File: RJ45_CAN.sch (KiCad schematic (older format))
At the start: 1 part, among them J1 RJ45

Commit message: Route, associate and generate bom and drawings.
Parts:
- J1: Farnell (none) -> 2135979
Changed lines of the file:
@@
 $Descr A4 11693 8268
 encoding utf-8
-Sheet 7 11
+Sheet 11 11
 Title ""
 Date "2021-02-26"
@@
 AR Path="/603AFD7E/603AEB0B" Ref="J9"  Part="1"
 AR Path="/603AFD80/603AEB0B" Ref="J10"  Part="1"
-F 0 "J6" H 5407 4367 50  0000 C CNN
+F 0 "J10" H 5407 4367 50  0000 C CNN
 F 1 "RJ45" H 5407 4276 50  0000 C CNN
 F 2 "Connector_RJ:RJ45_Amphenol_54602-x08_Horizontal" V 5350 3725 50  0001 C CNN
-F 3 "~" V 5350 3725 50  0001 C CNN
+F 3 "https://www.farnell.com/cad/1749592.pdf" V 5350 3725 50  0001 C CNN
+F 4 "2135979" H 5350 3700 50  0001 C CNN "Farnell"
 	1    5350 3700
 	1    0    0    -1

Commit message: Design v2 circuit and make footprints.
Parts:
- removed J1: RJ45, Connector_RJ:RJ45_Amphenol_54602-x08_Horizontal, symbol Connector:RJ45
- added J?: RJ45_Shielded, CAN-Distributor:RJHSE5480, symbol Connector:RJ45_Shielded
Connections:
- net labels added: CAN_SHLD
- net labels removed: CAN_V+, Reserved1, Reserved2, SHIELD
- wire segments 8 -> 7
- no-connect marks 0 -> 3
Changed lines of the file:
@@
 $Descr A4 11693 8268
 encoding utf-8
-Sheet 11 11
-Title ""
-Date "2021-02-26"
-Rev "1.0"
+Sheet 2 12
+Title "CAN Distributor"
+Date "2021-04-03"
+Rev "2.0"
 Comp ""
-Comment1 ""
+Comment1 "Designed by: Erik Almbratt"
 Comment2 ""
 Comment3 ""
 Comment4 ""
 $EndDescr
-$Comp
-L Connector:RJ45 J?
-U 1 1 603AEB0B
-P 5350 3700
-AR Path="/603AEB0B" Ref="J?"  Part="1"
-AR Path="/603ADFE4/603AEB0B" Ref="J1"  Part="1"
-AR Path="/603AF7AF/603AEB0B" Ref="J?"  Part="1"
-AR Path="/603AF7FC/603AEB0B" Ref="J2"  Part="1"
-AR Path="/603AF88D/603AEB0B" Ref="J3"  Part="1"
-AR Path="/603AF8B1/603AEB0B" Ref="J4"  Part="1"
-AR Path="/603AF8D1/603AEB0B" Ref="J5"  Part="1"
-AR Path="/603AF8E5/603AEB0B" Ref="J?"  Part="1"
-AR Path="/603AF91C/603AEB0B" Ref="J?"  Part="1"
-AR Path="/603AFD78/603AEB0B" Ref="J6"  Part="1"
-AR Path="/603AFD7A/603AEB0B" Ref="J7"  Part="1"
-AR Path="/603AFD7C/603AEB0B" Ref="J8"  Part="1"
-AR Path="/603AFD7E/603AEB0B" Ref="J9"  Part="1"
-AR Path="/603AFD80/603AEB0B" Ref="J10"  Part="1"
-F 0 "J10" H 5407 4367 50  0000 C CNN
-F 1 "RJ45" H 5407 4276 50  0000 C CNN
-F 2 "Connector_RJ:RJ45_Amphenol_54602-x08_Horizontal" V 5350 3725 50  0001 C CNN
-F 3 "https://www.farnell.com/cad/1749592.pdf" V 5350 3725 50  0001 C CNN
-F 4 "2135979" H 5350 3700 50  0001 C CNN "Farnell"
-	1    5350 3700
-	1    0    0    -1
-$EndComp
 Text GLabel 6100 4000 2    50   Input ~ 0
 CAN_H
@@
 CAN_GND
 Text GLabel 6100 3500 2    50   Input ~ 0
-SHIELD
-Text GLabel 6100 3700 2    50   Input ~ 0
-Reserved1
-Text GLabel 6100 3600 2    50   Input ~ 0
-Reserved2
-Text GLabel 6100 3300 2    50   Input ~ 0
-CAN_V+
-Wire Wire Line
-	6100 3300 5750 3300
+CAN_SHLD
 Wire Wire Line
 	5750 3400 6100 3400
 Wire Wire Line
 	6100 3500 5750 3500
-Wire Wire Line
-	5750 3600 6100 3600
-Wire Wire Line
-	6100 3700 5750 3700
 Wire Wire Line
 	5750 3800 6100 3800
@@
 Wire Wire Line
 	5750 4000 6100 4000
+NoConn ~ 5750 3300
+NoConn ~ 5750 3600
+NoConn ~ 5750 3700
+$Comp
+L Connector:RJ45_Shielded J?
+U 1 1 6068581B
+P 5350 3700
+AR Path="/603ADFE4/6068581B" Ref="J?"  Part="1"
+AR Path="/603AF7FC/6068581B" Ref="J?"  Part="1"
+AR Path="/603AF88D/6068581B" Ref="J?"  Part="1"
+AR Path="/603AF8B1/6068581B" Ref="J?"  Part="1"
+AR Path="/603AF8D1/6068581B" Ref="J?"  Part="1"
+AR Path="/603AFD78/6068581B" Ref="J?"  Part="1"
+AR Path="/603AFD7A/6068581B" Ref="J?"  Part="1"
+AR Path="/603AFD7C/6068581B" Ref="J?"  Part="1"
+AR Path="/603AFD7E/6068581B" Ref="J?"  Part="1"
+AR Path="/603AFD80/6068581B" Ref="J?"  Part="1"
+F 0 "J?" H 5350 4400 50  0000 C CNN
+F 1 "RJ45_Shielded" H 5350 4300 50  0000 C CNN
+F 2 "CAN-Distributor:RJHSE5480" V 5350 3725 50  0001 C CNN
+F 3 "https://www.farnell.com/cad/2360424.pdf" V 5350 3725 50  0001 C CNN
+F 4 "RJHSE5480" H 5350 3700 50  0001 C CNN "MPN"
+F 5 "3367703" H 5350 3700 50  0001 C CNN "Farnell"
+F 6 "AMPHENOL ICC" H 5350 3700 50  0001 C CNN "Manufacturer"
+	1    5350 3700
+	1    0    0    -1
+$EndComp
+Text GLabel 5500 4350 2    50   Input ~ 0
+CAN_SHLD
+Wire Wire Line
+	5350 4200 5350 4350
+Wire Wire Line
+	5350 4350 5500 4350
 $EndSCHEMATC

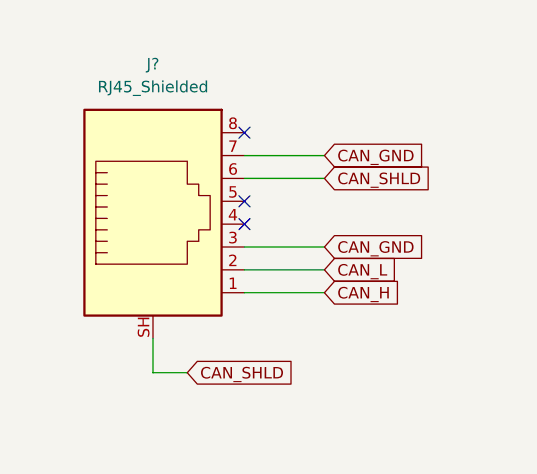
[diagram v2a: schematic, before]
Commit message: Perform layout. Add CAN testpoints.
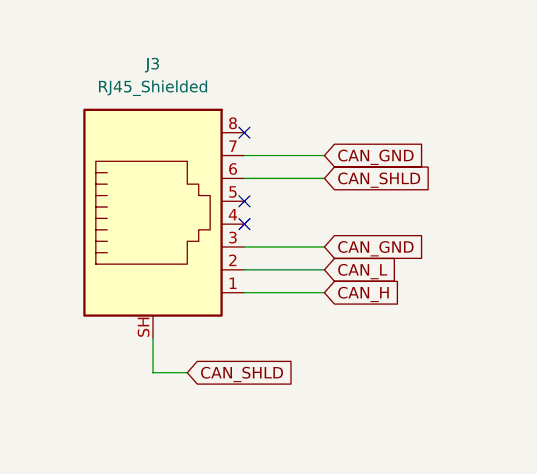
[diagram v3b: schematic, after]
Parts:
- gave numbers to parts that had none: 1
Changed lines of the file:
@@
 $Descr A4 11693 8268
 encoding utf-8
-Sheet 2 12
+Sheet 3 16
 Title "CAN Distributor"
 Date "2021-04-03"
@@
 NoConn ~ 5750 3700
 $Comp
-L Connector:RJ45_Shielded J?
+L Connector:RJ45_Shielded J2
 U 1 1 6068581B
 P 5350 3700
-AR Path="/603ADFE4/6068581B" Ref="J?"  Part="1"
-AR Path="/603AF7FC/6068581B" Ref="J?"  Part="1"
+AR Path="/603ADFE4/6068581B" Ref="J2"  Part="1"
+AR Path="/603AF7FC/6068581B" Ref="J3"  Part="1"
 AR Path="/603AF88D/6068581B" Ref="J?"  Part="1"
 AR Path="/603AF8B1/6068581B" Ref="J?"  Part="1"
@@
 AR Path="/603AFD7E/6068581B" Ref="J?"  Part="1"
 AR Path="/603AFD80/6068581B" Ref="J?"  Part="1"
-F 0 "J?" H 5350 4400 50  0000 C CNN
+F 0 "J3" H 5350 4400 50  0000 C CNN
 F 1 "RJ45_Shielded" H 5350 4300 50  0000 C CNN
 F 2 "CAN-Distributor:RJHSE5480" V 5350 3725 50  0001 C CNN

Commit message: Add protection TVS and GDT. Rename TP file.
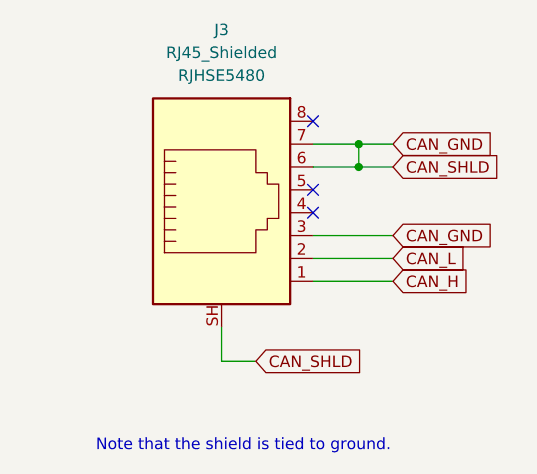
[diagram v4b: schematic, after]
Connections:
- net CAN_SHLD is gone; now on net CAN_GND: J2.6, J2.SH
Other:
- note added: "Note that the shield is tied to ground."
- moved on the sheet: J3
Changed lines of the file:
@@
 Sheet 3 16
 Title "CAN Distributor"
-Date "2021-04-03"
-Rev "2.0"
+Date "2021-04-04"
+Rev "2.1"
 Comp ""
 Comment1 "Designed by: Erik Almbratt"
@@
 Comment4 ""
 $EndDescr
-Text GLabel 6100 4000 2    50   Input ~ 0
-CAN_H
-Text GLabel 6100 3900 2    50   Input ~ 0
-CAN_L
-Text GLabel 6100 3800 2    50   Input ~ 0
+Text GLabel 6400 3750 2    50   Input ~ 0
 CAN_GND
-Text GLabel 6100 3400 2    50   Input ~ 0
+Text GLabel 6400 3350 2    50   Input ~ 0
 CAN_GND
-Text GLabel 6100 3500 2    50   Input ~ 0
-CAN_SHLD
 Wire Wire Line
-	5750 3400 6100 3400
-Wire Wire Line
-	6100 3500 5750 3500
-Wire Wire Line
-	5750 3800 6100 3800
-Wire Wire Line
-	6100 3900 5750 3900
-Wire Wire Line
-	5750 4000 6100 4000
-NoConn ~ 5750 3300
-NoConn ~ 5750 3600
-NoConn ~ 5750 3700
+	6050 3750 6400 3750
+NoConn ~ 6050 3250
+NoConn ~ 6050 3550
+NoConn ~ 6050 3650
 $Comp
 L Connector:RJ45_Shielded J2
 U 1 1 6068581B
-P 5350 3700
+P 5650 3650
 AR Path="/603ADFE4/6068581B" Ref="J2"  Part="1"
 AR Path="/603AF7FC/6068581B" Ref="J3"  Part="1"
@@
 AR Path="/603AFD7E/6068581B" Ref="J?"  Part="1"
 AR Path="/603AFD80/6068581B" Ref="J?"  Part="1"
-F 0 "J3" H 5350 4400 50  0000 C CNN
-F 1 "RJ45_Shielded" H 5350 4300 50  0000 C CNN
-F 2 "CAN-Distributor:RJHSE5480" V 5350 3725 50  0001 C CNN
-F 3 "https://www.farnell.com/cad/2360424.pdf" V 5350 3725 50  0001 C CNN
-F 4 "RJHSE5480" H 5350 3700 50  0001 C CNN "MPN"
-F 5 "3367703" H 5350 3700 50  0001 C CNN "Farnell"
-F 6 "AMPHENOL ICC" H 5350 3700 50  0001 C CNN "Manufacturer"
-	1    5350 3700
+F 0 "J3" H 5650 4450 50  0000 C CNN
+F 1 "RJ45_Shielded" H 5650 4350 50  0000 C CNN
+F 2 "CAN-Distributor:RJHSE5480" V 5650 3675 50  0001 C CNN
+F 3 "https://www.farnell.com/cad/2360424.pdf" V 5650 3675 50  0001 C CNN
+F 4 "RJHSE5480" H 5650 4250 50  0000 C CNN "MPN"
+F 5 "3367703" H 5650 3650 50  0001 C CNN "Farnell"
+F 6 "AMPHENOL ICC" H 5650 3650 50  0001 C CNN "Manufacturer"
+	1    5650 3650
 	1    0    0    -1
 $EndComp
-Text GLabel 5500 4350 2    50   Input ~ 0
+Wire Wire Line
+	5650 4150 5650 4300
+Wire Wire Line
+	5650 4300 5800 4300
+Text GLabel 5800 4300 2    50   Input ~ 0
+CAN_SHLD
+Text GLabel 6400 3450 2    50   Input ~ 0
 CAN_SHLD
 Wire Wire Line
-	5350 4200 5350 4350
+	6250 3350 6400 3350
 Wire Wire Line
-	5350 4350 5500 4350
+	6050 3350 6250 3350
+Connection ~ 6250 3350
+Wire Wire Line
+	6250 3450 6050 3450
+Wire Wire Line
+	6400 3450 6250 3450
+Connection ~ 6250 3450
+Wire Wire Line
+	6250 3450 6250 3350
+Wire Wire Line
+	6050 3950 6400 3950
+Wire Wire Line
+	6050 3850 6400 3850
+Text GLabel 6400 3850 2    50   Input ~ 0
+CAN_L
+Text GLabel 6400 3950 2    50   Input ~ 0
+CAN_H
+Text Notes 5100 4700 0    50   ~ 0
+Note that the shield is tied to ground.
 $EndSCHEMATC
